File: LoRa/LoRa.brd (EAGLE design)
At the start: 59.4 x 27.9 mm, 33 parts, among them J1 UP2-AH-1-TH, U1 STM32L053C8T6, U2 RFM69HCW, U5 LM3671MF-3.3/NOPB, X1 uFL/SMA, Y1 ECS-80-S-4X

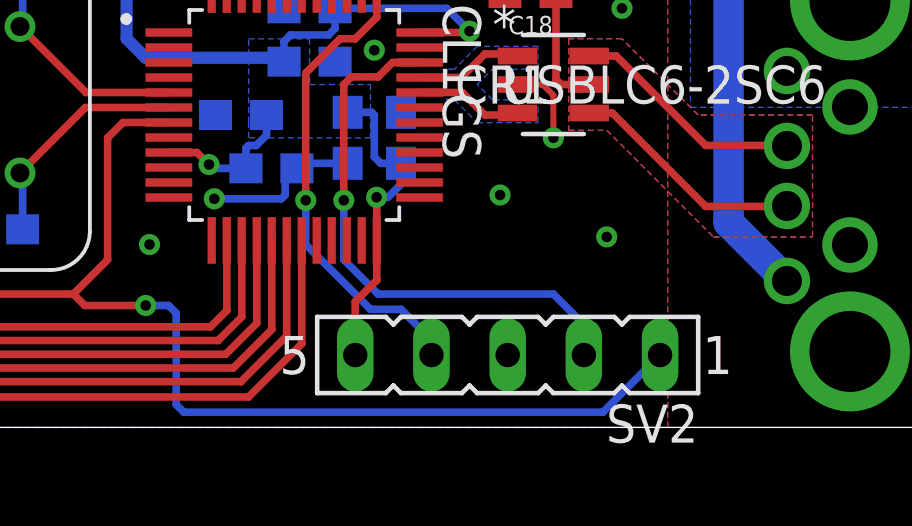
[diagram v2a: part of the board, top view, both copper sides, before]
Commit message: added led indicator
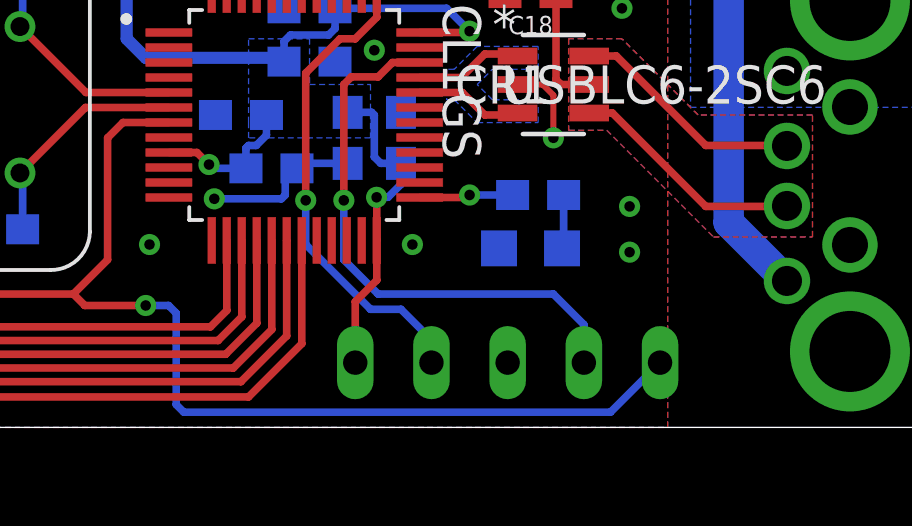
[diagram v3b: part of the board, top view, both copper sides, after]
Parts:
- added LED1: (no value), led:CHIP-LED0805
- added R2: 1k, SparkFun-Resistors:0603
- moved SV2 0.25 mm to (45.5, 2.16), flipped to the bottom, turned to 0 degrees
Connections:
- new net N$3: R2.2, U1.25
- new net N$4: LED1.A, R2.1
- net GND: now also LED1.C
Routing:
- net N$3: track 0.00 -> 3.13 mm, vias 0 -> 1
- net N$4: track 0.00 -> 1.80 mm
- net GND: vias 32 -> 33
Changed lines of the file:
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@@
 <setting verticaltext="up"/>
 </settings>
-<grid distance="10" unitdist="mil" unit="mil" style="lines" multiple="1" display="yes" altdistance="5" altunitdist="mil" altunit="mil"/>
+<grid distance="5" unitdist="mil" unit="mil" style="lines" multiple="1" display="yes" altdistance="5" altunitdist="mil" altunit="mil"/>
 <layers>
 <layer number="1" name="Top" color="4" fill="1" visible="yes" active="yes"/>
@@
 <attribute name="PROD_ID" value="CAP-00868" x="34.544" y="18.034" size="1.778" layer="28" rot="MR90" display="off"/>
 </element>
-<element name="SV2" library="con-lsta" library_urn="urn:adsk.eagle:library:161" package="FE05-1" package3d_urn="urn:adsk.eagle:package:8190/1" value="" x="45.466" y="2.413" rot="R180">
-<attribute name="MF" value="" x="45.466" y="2.413" size="1.778" layer="27" rot="R180" display="off"/>
-<attribute name="MPN" value="" x="45.466" y="2.413" size="1.778" layer="27" rot="R180" display="off"/>
-<attribute name="OC_FARNELL" value="unknown" x="45.466" y="2.413" size="1.778" layer="27" rot="R180" display="off"/>
-<attribute name="OC_NEWARK" value="unknown" x="45.466" y="2.413" size="1.778" layer="27" rot="R180" display="off"/>
+<element name="SV2" library="con-lsta" library_urn="urn:adsk.eagle:library:161" package="FE05-1" package3d_urn="urn:adsk.eagle:package:8190/1" value="" x="45.466" y="2.159" rot="MR0">
+<attribute name="MF" value="" x="45.466" y="2.159" size="1.778" layer="28" rot="MR0" display="off"/>
+<attribute name="MPN" value="" x="45.466" y="2.159" size="1.778" layer="28" rot="MR0" display="off"/>
+<attribute name="OC_FARNELL" value="unknown" x="45.466" y="2.159" size="1.778" layer="28" rot="MR0" display="off"/>
+<attribute name="OC_NEWARK" value="unknown" x="45.466" y="2.159" size="1.778" layer="28" rot="MR0" display="off"/>
 </element>
 <element name="U5" library="microbuilder" package="SOT23-5" value="LM3671MF-3.3/NOPB" x="54.102" y="23.876" rot="R90"/>
@@
 <element name="J2" library="SparkFun-Connectors" library_urn="urn:adsk.eagle:library:513" package="1X03" package3d_urn="urn:adsk.eagle:package:38063/1" value="" x="24.511" y="22.098"/>
 <element name="J3" library="SparkFun-Connectors" library_urn="urn:adsk.eagle:library:513" package="1X03" package3d_urn="urn:adsk.eagle:package:38063/1" value="" x="24.511" y="26.162"/>
+<element name="LED1" library="led" library_urn="urn:adsk.eagle:library:259" package="CHIP-LED0805" package3d_urn="urn:adsk.eagle:package:15818/2" value="" x="46.228" y="5.969" rot="MR270">
+<attribute name="SPICEPREFIX" value="L" x="46.228" y="5.969" size="1.778" layer="28" rot="MR270" display="off"/>
+</element>
+<element name="R2" library="SparkFun-Resistors" library_urn="urn:adsk.eagle:library:532" package="0603" package3d_urn="urn:adsk.eagle:package:39650/1" value="1k" x="46.482" y="7.747" rot="MR0">
+<attribute name="PROD_ID" value="RES-07856" x="46.482" y="7.747" size="1.778" layer="28" rot="MR0" display="off"/>
+</element>
 </elements>
 <signals>
@@
 <wire x1="37.925" y1="7.62" x2="35.687" y2="7.62" width="0.254" layer="16"/>
 <via x="42.672" y="15.113" extent="1-16" drill="0.35"/>
-<via x="45.212" y="7.747" extent="1-16" drill="0.35"/>
 <wire x1="41.91" y1="10.502" x2="41.783" y2="10.629" width="0.254" layer="16"/>
 <via x="41.021" y="12.573" extent="1-16" drill="0.35"/>
@@
 <via x="3.048" y="16.002" extent="1-16" drill="0.35"/>
 <via x="37.592" y="20.32" extent="1-16" drill="0.35"/>
-<via x="48.768" y="6.35" extent="1-16" drill="0.35"/>
+<via x="49.53" y="7.366" extent="1-16" drill="0.35"/>
 <via x="33.528" y="6.096" extent="1-16" drill="0.35"/>
 <polygon width="0.2032" layer="1" rank="4">
@@
 <via x="39.624" y="20.32" extent="1-16" drill="0.35"/>
 <via x="52.451" y="19.558" extent="1-16" drill="0.35"/>
+<via x="49.53" y="5.842" extent="1-16" drill="0.35"/>
+<via x="42.291" y="6.096" extent="1-16" drill="0.35"/>
+<contactref element="LED1" pad="C"/>
 </signal>
 <signal name="3.3V">
@@
 <wire x1="41.104" y1="6.234" x2="41.104" y2="4.909" width="0.254" layer="1"/>
 <wire x1="41.104" y1="4.909" x2="40.386" y2="4.191" width="0.254" layer="1"/>
-<wire x1="40.386" y1="4.191" x2="40.386" y2="2.413" width="0.254" layer="1"/>
 <wire x1="39.712" y1="13.97" x2="43.434" y2="13.97" width="0.254" layer="16"/>
 <wire x1="43.434" y1="13.97" x2="44.196" y2="13.208" width="0.254" layer="16"/>
@@
 <wire x1="44.3103" y1="25.0450875" x2="44.3103" y2="24.6126" width="1.016" layer="1"/>
 <wire x1="44.3103" y1="24.6126" x2="43.942" y2="24.2443" width="1.016" layer="1"/>
+<wire x1="40.386" y1="4.191" x2="40.386" y2="2.159" width="0.254" layer="1"/>
 <wire x1="49.059" y1="23.622" x2="52.8019" y2="24.826" width="0" layer="19" extent="1-1"/>
 </signal>
@@
 <wire x1="38.735" y1="7.57" x2="38.735" y2="6.096" width="0.254" layer="16"/>
 <wire x1="40.894" y1="3.937" x2="41.91" y2="3.937" width="0.254" layer="16"/>
-<wire x1="41.91" y1="3.937" x2="42.926" y2="2.921" width="0.254" layer="16"/>
-<wire x1="42.926" y1="2.921" x2="42.926" y2="2.413" width="0.254" layer="16"/>
+<wire x1="42.926" y1="2.921" x2="41.91" y2="3.937" width="0.254" layer="16"/>
 <wire x1="38.735" y1="6.096" x2="40.894" y2="3.937" width="0.254" layer="16"/>
+<wire x1="42.926" y1="2.159" x2="42.926" y2="2.921" width="0.254" layer="16"/>
 </signal>
 <signal name="SWDIO">
@@
 <wire x1="41.148" y1="4.445" x2="46.99" y2="4.445" width="0.254" layer="16"/>
 <wire x1="46.99" y1="4.445" x2="48.006" y2="3.429" width="0.254" layer="16"/>
-<wire x1="48.006" y1="3.429" x2="48.006" y2="2.413" width="0.254" layer="16"/>
 <wire x1="40.005" y1="5.588" x2="41.148" y2="4.445" width="0.254" layer="16"/>
 <wire x1="42.534" y1="12.164" x2="41.628" y2="12.164" width="0.254" layer="1"/>
@@
 <wire x1="41.148" y1="11.684" x2="40.259" y2="11.684" width="0.254" layer="1"/>
 <wire x1="40.259" y1="11.684" x2="40.005" y2="11.43" width="0.254" layer="1"/>
+<wire x1="48.006" y1="3.429" x2="48.006" y2="2.159" width="0.254" layer="16"/>
 </signal>
 <signal name="NRST">
@@
 <wire x1="34.417" y1="3.81" x2="34.417" y2="0.762" width="0.254" layer="16"/>
 <wire x1="34.417" y1="0.762" x2="34.671" y2="0.508" width="0.254" layer="16"/>
-<wire x1="34.671" y1="0.508" x2="48.641" y2="0.508" width="0.254" layer="16"/>
-<wire x1="48.641" y1="0.508" x2="50.546" y2="2.413" width="0.254" layer="16"/>
 <wire x1="22.86" y1="12.485" x2="22.86" y2="11.43" width="0.254" layer="16"/>
 <via x="22.86" y="11.43" extent="1-16" drill="0.35"/>
 <wire x1="22.86" y1="11.43" x2="22.86" y2="9.773" width="0.254" layer="1"/>
+<wire x1="48.895" y1="0.508" x2="50.546" y2="2.159" width="0.254" layer="16"/>
+<wire x1="34.671" y1="0.508" x2="48.895" y2="0.508" width="0.254" layer="16"/>
 </signal>
 <signal name="N$2">
@@
 </polygon>
 </signal>
+<signal name="N$3">
+<contactref element="U1" pad="25"/>
+<contactref element="R2" pad="2"/>
+<wire x1="42.534" y1="7.664" x2="44.113" y2="7.664" width="0.254" layer="1"/>
+<wire x1="44.113" y1="7.664" x2="44.196" y2="7.747" width="0.254" layer="1"/>
+<via x="44.196" y="7.747" extent="1-16" drill="0.35"/>
+<wire x1="44.196" y1="7.747" x2="45.632" y2="7.747" width="0.254" layer="16"/>
+</signal>
+<signal name="N$4">
+<contactref element="R2" pad="1"/>
+<contactref element="LED1" pad="A"/>
+<wire x1="47.332" y1="7.747" x2="47.332" y2="6.023" width="0.254" layer="16"/>
+<wire x1="47.332" y1="6.023" x2="47.278" y2="5.969" width="0.254" layer="16"/>
+</signal>
 </signals>
